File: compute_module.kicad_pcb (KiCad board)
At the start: 4 copper layers, 93.2 x 51.6 mm, 43 parts, among them J1 2001-1-2-21-00-BK, P1 POWER, P2 HOST, P3 CAM1, Q1 2N7002P.215, Q2 DMP3056L-7, Q3 2N7002P.215, U1 REG1117-3.3, U3 REG1117A-1.8

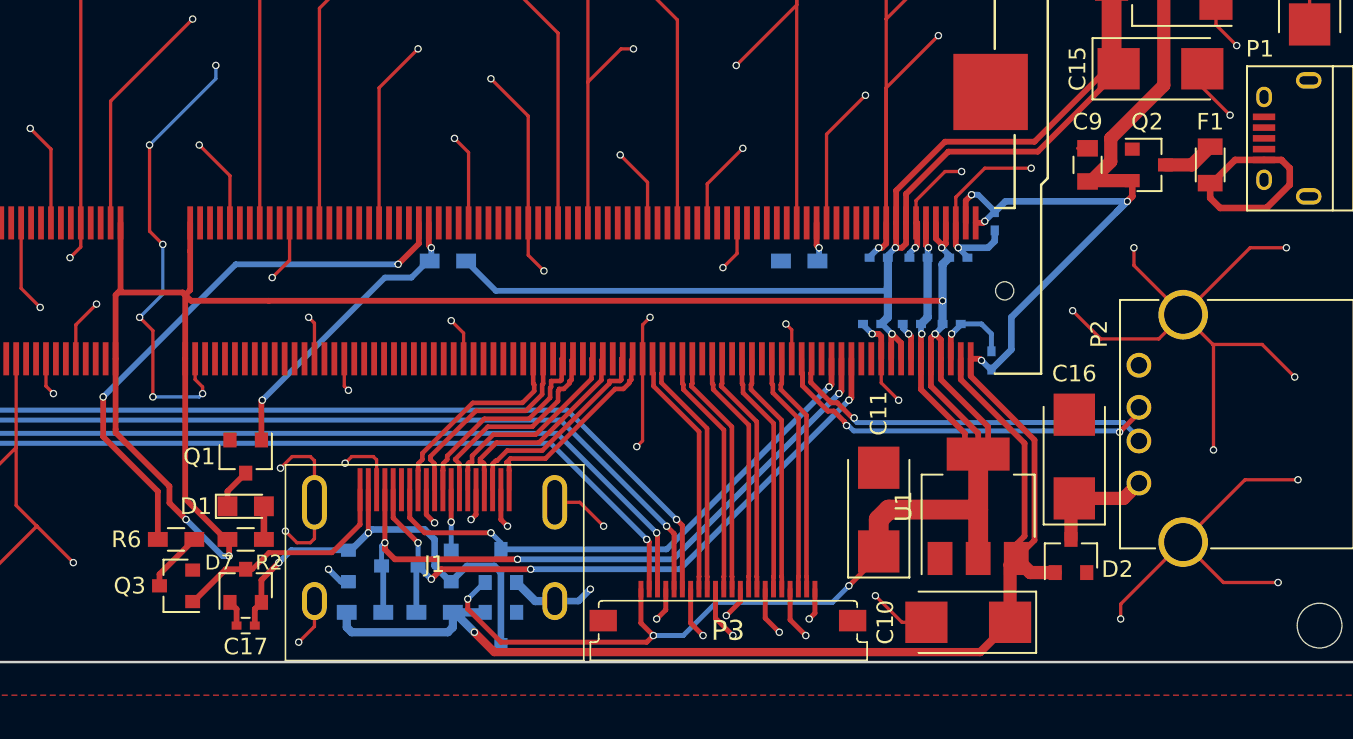
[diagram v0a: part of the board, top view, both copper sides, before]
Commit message: Added decoupling caps for gpio power pins
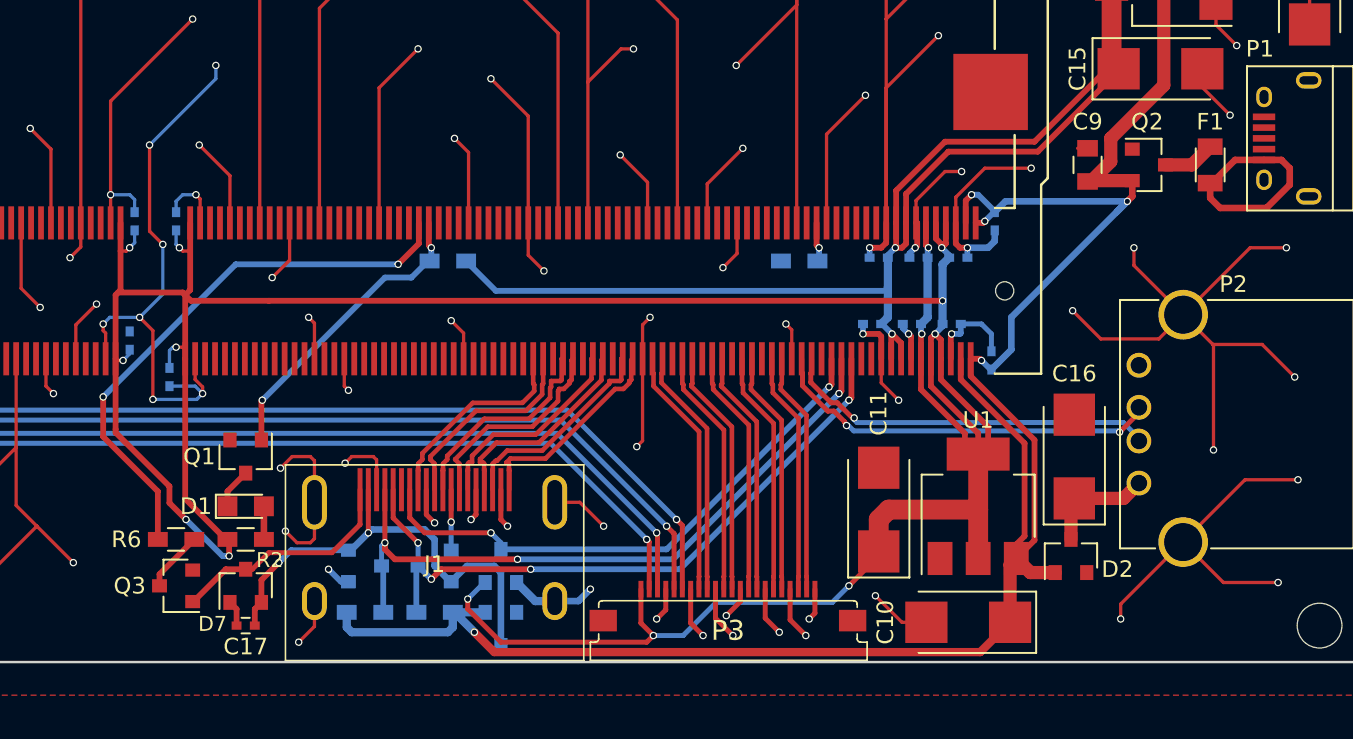
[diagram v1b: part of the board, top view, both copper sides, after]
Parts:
- added C12: 100nF, Capacitors_SMD:C_0402, B.Cu at (107.1, 79.8)
- added C13: 100nF, Capacitors_SMD:C_0402, B.Cu at (109.6, 79.8)
- added C18: 100nF, Capacitors_SMD:C_0402, B.Cu at (106.8, 87.0)
- added C19: 100nF, Capacitors_SMD:C_0402, B.Cu at (109.2, 89.2)
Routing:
- net GND: track 559.4 -> 573.4 mm, vias 86 -> 89
- net +3V3: track 184.4 -> 192.0 mm, vias 10 -> 14

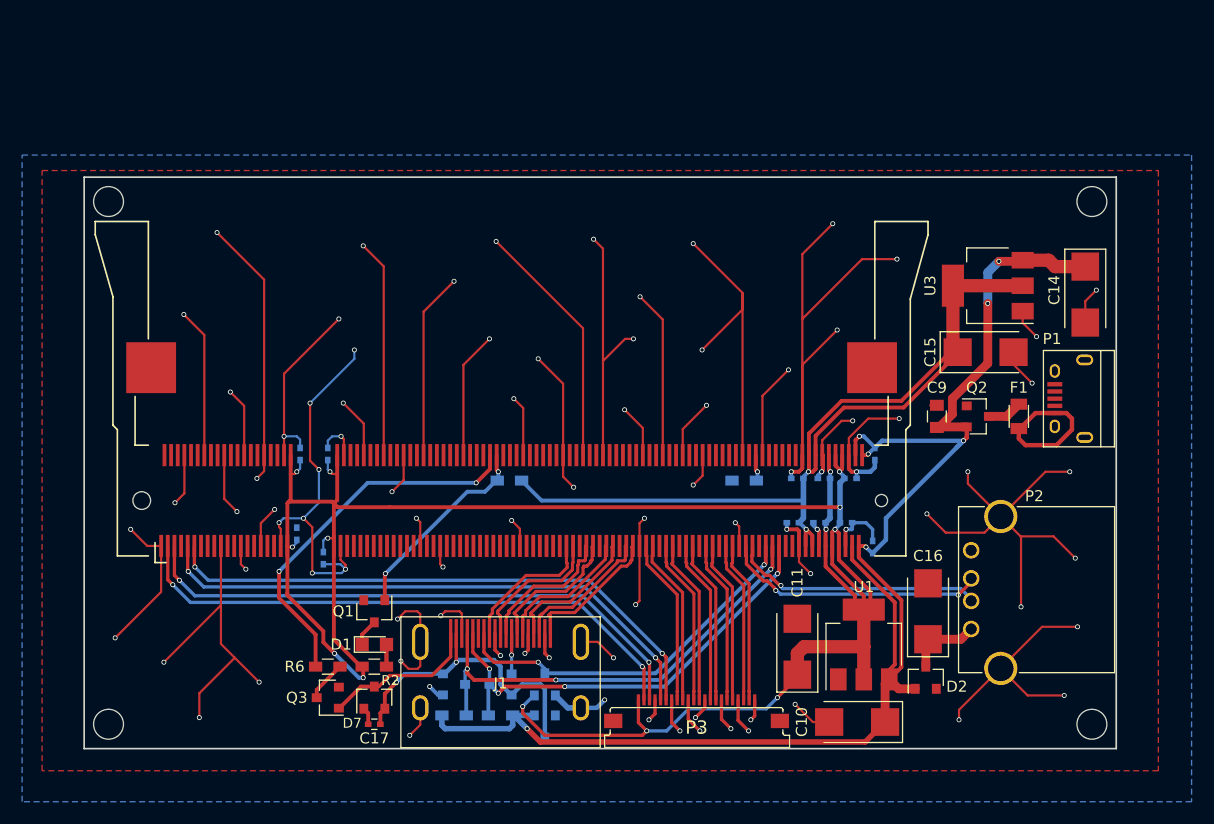
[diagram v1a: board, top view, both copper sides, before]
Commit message: Added pull-ups for gpio28, 29, 44 and 45
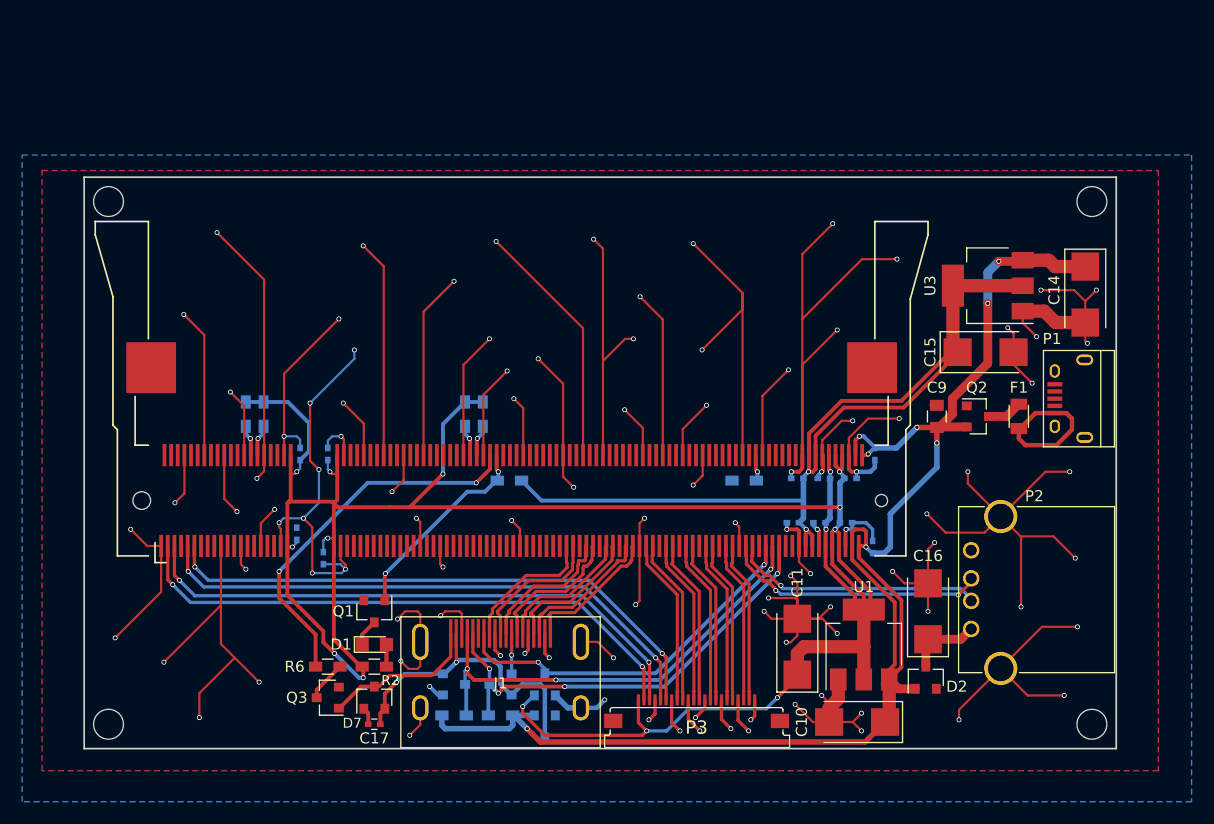
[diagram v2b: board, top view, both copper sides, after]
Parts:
- added R10: 10K, Resistors_SMD:R_0603_HandSoldering, B.Cu at (102.2, 76.2)
- added R7: 10K, Resistors_SMD:R_0603_HandSoldering, B.Cu at (123.6, 76.2)
- added R8: 10K, Resistors_SMD:R_0603_HandSoldering, B.Cu at (122.0, 76.2)
- added R9: 10K, Resistors_SMD:R_0603_HandSoldering, B.Cu at (103.8, 76.2)
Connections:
- MD1 pad 28: Net-(MD1-Pad28) -> GPIO28
- MD1 pad 30: Net-(MD1-Pad30) -> GPIO29
- MD1 pad 82: Net-(MD1-Pad82) -> GPIO44
- MD1 pad 84: Net-(MD1-Pad84) -> GPIO45
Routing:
- net GND: track 573.4 -> 644.6 mm, vias 89 -> 105
- net +3V3: track 192.0 -> 215.4 mm, vias 14 -> 15
- net GPIO45: track 0.00 -> 2.83 mm, vias 0 -> 1
- net GPIO29: track 0.00 -> 2.83 mm, vias 0 -> 1
- net GPIO44: track 0.00 -> 2.79 mm, vias 0 -> 1
- net GPIO28: track 0.00 -> 2.79 mm, vias 0 -> 1
- net +5V: track 139.7 -> 141.0 mm, vias 7 -> 8

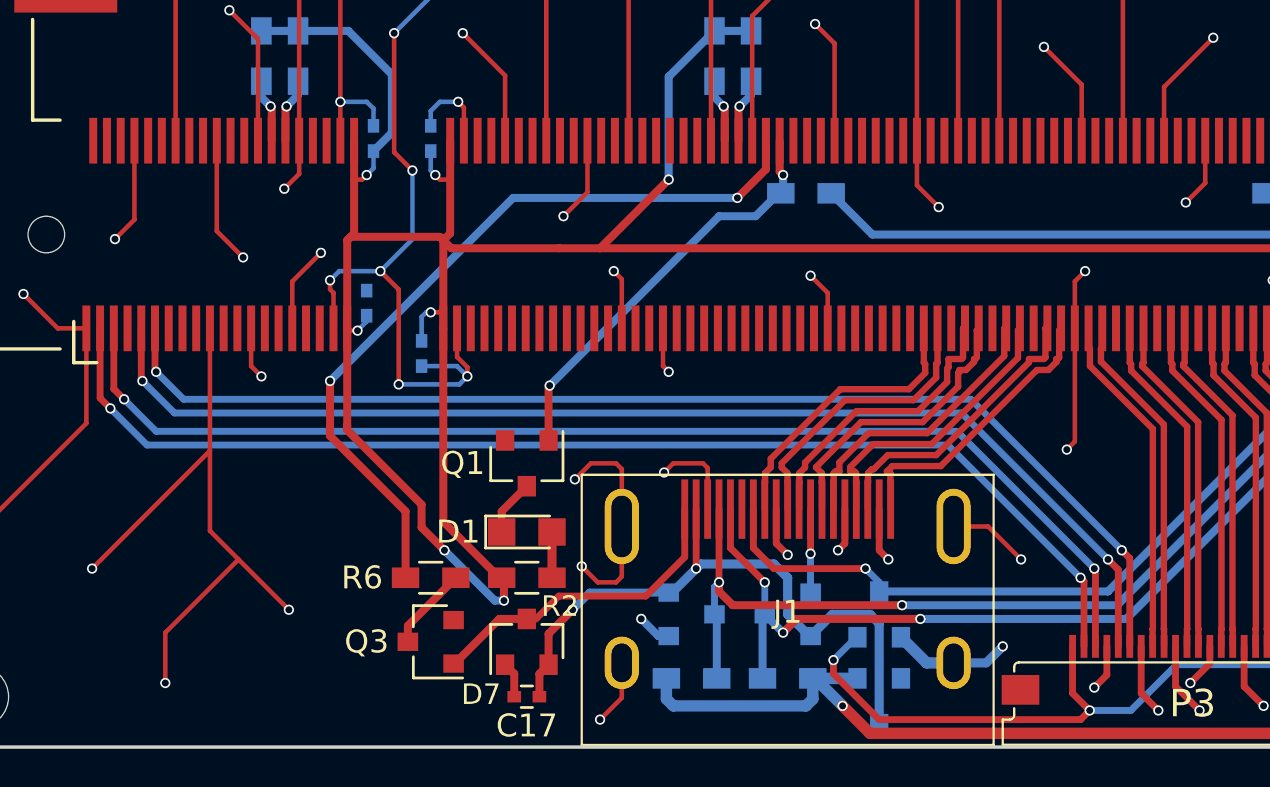
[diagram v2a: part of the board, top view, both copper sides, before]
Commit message: Moved CAM1_IO0 and CAM1_IO1 to gpio 31 and 30
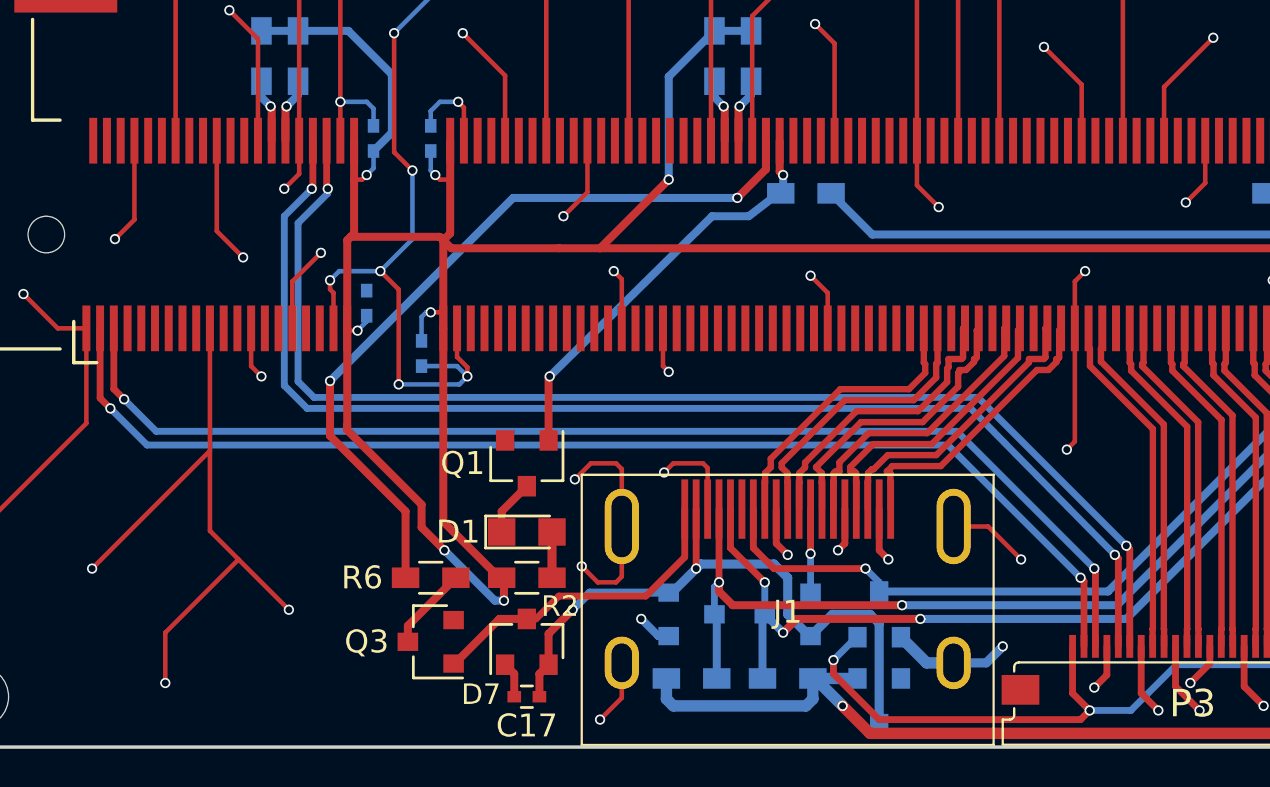
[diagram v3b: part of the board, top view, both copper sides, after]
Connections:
- MD1 pad 11: CAM1_IO0 -> Net-(MD1-Pad11)
- MD1 pad 34: Net-(MD1-Pad34) -> CAM1_IO1
- MD1 pad 36: Net-(MD1-Pad36) -> CAM1_IO0
- MD1 pad 9: CAM1_IO1 -> Net-(MD1-Pad9)
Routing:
- net CAM1_IO0: track 51.7 -> 54.7 mm
- net CAM1_IO1: track 51.7 -> 54.7 mm

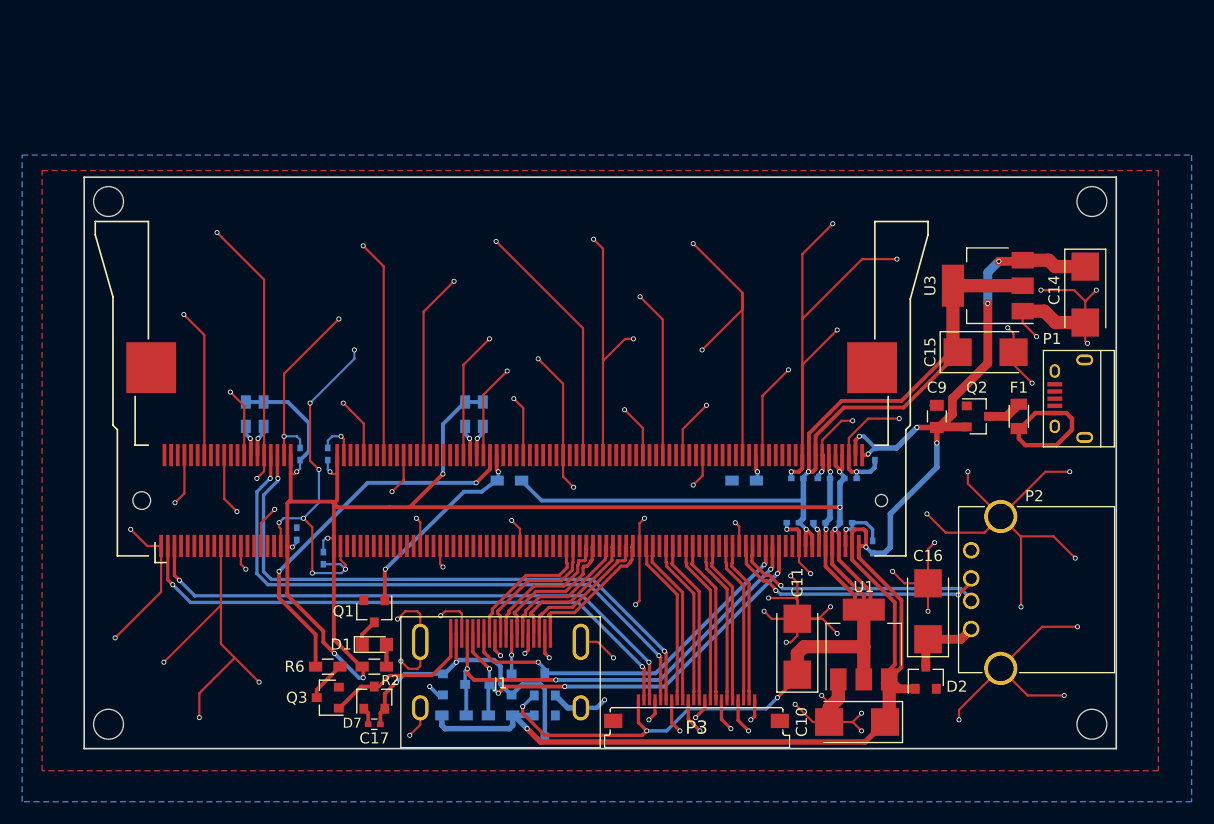
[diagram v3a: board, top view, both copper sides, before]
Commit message: Partially routed gpio header
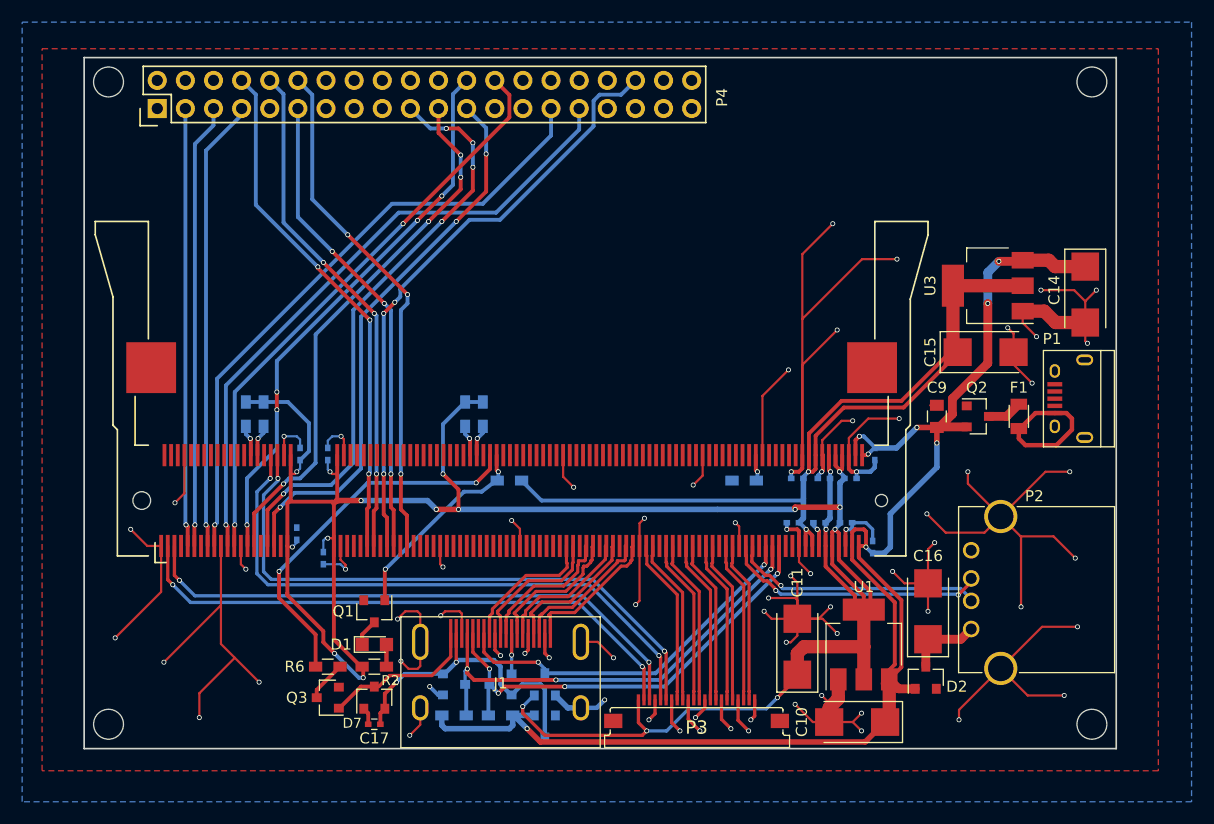
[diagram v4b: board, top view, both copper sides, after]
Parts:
- added P4: CONN_02X20, Pin_Headers:Pin_Header_Straight_2x20, F.Cu at (94.2, 48.6)
- moved REF** 10.8 mm to (178.6, 46.2)
- moved REF** 10.8 mm to (89.8, 46.2)
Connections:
- MD1 pad 11: Net-(MD1-Pad11) -> GPIO3
- MD1 pad 15: Net-(MD1-Pad15) -> GPIO4
- MD1 pad 17: Net-(MD1-Pad17) -> GPIO5
- MD1 pad 21: Net-(MD1-Pad21) -> GPIO6
- MD1 pad 23: Net-(MD1-Pad23) -> GPIO7
- MD1 pad 27: Net-(MD1-Pad27) -> GPIO8
- MD1 pad 29: Net-(MD1-Pad29) -> GPIO9
- MD1 pad 33: Net-(MD1-Pad33) -> GPIO10
- MD1 pad 35: Net-(MD1-Pad35) -> GPIO11
- MD1 pad 45: Net-(MD1-Pad45) -> GPIO12
- MD1 pad 47: Net-(MD1-Pad47) -> GPIO13
- MD1 pad 51: Net-(MD1-Pad51) -> GPIO14
- MD1 pad 53: Net-(MD1-Pad53) -> GPIO15
- MD1 pad 57: Net-(MD1-Pad57) -> GPIO16
- MD1 pad 59: Net-(MD1-Pad59) -> GPIO17
- MD1 pad 63: Net-(MD1-Pad63) -> GPIO18
- MD1 pad 65: Net-(MD1-Pad65) -> GPIO19
- MD1 pad 69: Net-(MD1-Pad69) -> GPIO20
- MD1 pad 71: Net-(MD1-Pad71) -> GPIO21
- MD1 pad 75: Net-(MD1-Pad75) -> GPIO22
- MD1 pad 77: Net-(MD1-Pad77) -> GPIO23
- MD1 pad 81: Net-(MD1-Pad81) -> GPIO24
- MD1 pad 83: Net-(MD1-Pad83) -> GPIO25
- MD1 pad 87: Net-(MD1-Pad87) -> GPIO26
- MD1 pad 89: Net-(MD1-Pad89) -> GPIO27
- MD1 pad 9: Net-(MD1-Pad9) -> GPIO2
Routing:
- net GND: track 644.6 -> 365.7 mm, vias 105 -> 75
- net GPIO6: track 0.00 -> 57.9 mm, vias 0 -> 1
- net GPIO5: track 0.00 -> 56.9 mm, vias 0 -> 1
- net GPIO16: track 0.00 -> 54.4 mm, vias 0 -> 3
- net GPIO10: track 0.00 -> 53.1 mm, vias 0 -> 5
- net GPIO7: track 0.00 -> 52.9 mm, vias 0 -> 2
- net GPIO11: track 0.00 -> 50.4 mm, vias 0 -> 3
- net GPIO8: track 0.00 -> 50.3 mm, vias 0 -> 5
- net GPIO9: track 0.00 -> 48.6 mm, vias 0 -> 4
- net GPIO14: track 0.00 -> 46.9 mm, vias 0 -> 3
- net GPIO18: track 0.00 -> 46.6 mm, vias 0 -> 3
- net GPIO15: track 0.00 -> 46.1 mm, vias 0 -> 3
- net GPIO17: track 0.00 -> 43.1 mm, vias 0 -> 3
- net GPIO4: track 0.00 -> 40.9 mm, vias 0 -> 1
- net GPIO3: track 0.00 -> 40.2 mm, vias 0 -> 1
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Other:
- board size 93.2 x 51.6 mm -> 93.2 x 62.4 mm
